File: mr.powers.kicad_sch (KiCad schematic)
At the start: 0 parts

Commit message: Place Holder:
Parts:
- added C1, C3, C4, C5: C, symbol pspice:C
- added D1: 12VAC RED, symbol Device:LED
- added D2: LED, symbol Device:LED
- added HS1: Heatsink, symbol Mechanical:Heatsink
- added R1: 100W 8Ohms, symbol Device:R
- added R2, R3, R4: 0Ω, symbol Device:R
- added R6: 1MΩ, symbol Device:R
- added R8: R, symbol Device:R
- added SW1: SW_SPST, symbol Switch:SW_SPST
- added U2: Antec 400W, symbol bvm-library:PSU
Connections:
- new net: R8.2, U2. (VDC_PSU_GND)
- new net 120VAC_SUPPLY_L: C1.1, C4.1, D1.2 (A), R2.1, R6.2
- new net 120VAC_SUPPLY_N: C1.2, C3.1, D1.1 (K), R3.1, R6.1
- new net 12VDC_SUPPLY: C5.2, U2. (VDC_PSU_GND)
- new net 3.3VDC_SUPPLY: U2. (VDC_PSU_GND)
- new net 5VDC_SB_SUPPLY: D2.2 (A), U2. (VDC_PSU_GND)
- new net 5VDC_SUPPLY: R1.1, R1.2, U2. (VDC_PSU_GND)
- new net Earth: R4.2, U2. (VDC_PSU_GND)
- new net NEUT: R3.2, U2. (VDC_PSU_GND)
- new net VAC: SW1.1 (A)
- new net VAC_GROUND: C3.2, C4.2, R4.1
- new net VAC_LINE_IN: R2.2, SW1.2 (B), U2. (VDC_PSU_GND)
- new net VDC_GND: C5.1, D2.1 (K), R8.1, U2. (VDC_PSU_GND)
- no-connect marks 2 -> 3
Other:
- sheet Mr. Power Meter renamed Mr. Power Meter Module
- added sheet 12VDC External Supply (12VDC External Supply.kicad_sch)
- note added: "-5VDC (White x1)"
- note added: "AC Power Meter of Mr Power's power. Current measurement taken before PSU using closed toroidal coil."
- note added: "DC power meter, shunted. Passes external DC power through and measurse it before passing it back out."
- note added: "FUSED"
- note added: "GFCI Will be added prior to PSU connection."
- note added: "Initial Condition Plugged in. PSU switch: Off: Everything is off, all switches in their off state. Action -> PSU Switch: On [PSU Power Switch] Result -> Ready LED turns on (GREEN) -> Always on USB charge ports 5V/2A and indicator turn on (GREEN) Action -> SYS Power: On [Top left panel] Result -> Sys Power Switch Lights Up -> System Power Monitor turns on -> Fans start -> AC Active Indicator (YELL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"
- note added: "Mr. Power Standby LED (Green)"
- note added: "PSU Mains Switch"
- note added: "PSU Needs a minimal load to before it will turn on. Is this true?"
- note added: "Since we need to modify he PSU to expose the AC lines and put a current sensor around the input AC lines, we're showing tha physical seperation between the PSU's switch and internal circuitry."
- note added: "Y Cap?"
- note added: "[AC LIVE INDICATOR]"
- note added: "https://www.smpspowersupply.com/connectors-pinouts.html"
- note added: "nPS_ON (Green x1)"
- note removed: "-5VDC ?? (White x1)"
- note removed: "120VAC_INT_SUPPLY_LIVE"
- note removed: "120VAC_INT_SUPPLY_NUETRAL"
- note removed: "AC Digital Meter (D85-2058) Hall Effect: AC 40V-300V, 0A - 100A"
- note removed: "AC Power Meter (KWS-AC300-100A) Hall Effect: AC 50V-300V 0A-100A"
- note removed: "DC Meter: (PZEM-051) Shunt: DC 6.5V-100V 0A-100A"
- note removed: "Initial Condition Pluged in. PSU switch: Off: Everything is off, all switches in their off state. Action -> PSU Switch: On Result -> Ready LED turns on -> Always on USB charge ports 5V/2A and indicator turn on Action -> SYS Power: On Result -> Switch Lights Up -> System Power Monitor turns on -> Fans start Action -> 12V Switch: On Result -> 12V monitor turns on -> 12V terminals "live" The same pa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"
- note removed: "PS_ON (Green x1)"
- note removed: "VAC_GROUND"
- note removed: "[4] DC Meter: (YB27VA) Shunt: DC 0V-100V 0A-50A"

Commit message: Draft 5VDC Supply Schematic
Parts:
- removed C5: C, symbol pspice:C
- D2: value LED -> 5VDC GREEN
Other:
- note added: "[STANDBY ACTIVE INDICATOR]"
- note removed: "Mr. Power Standby LED (Green)"

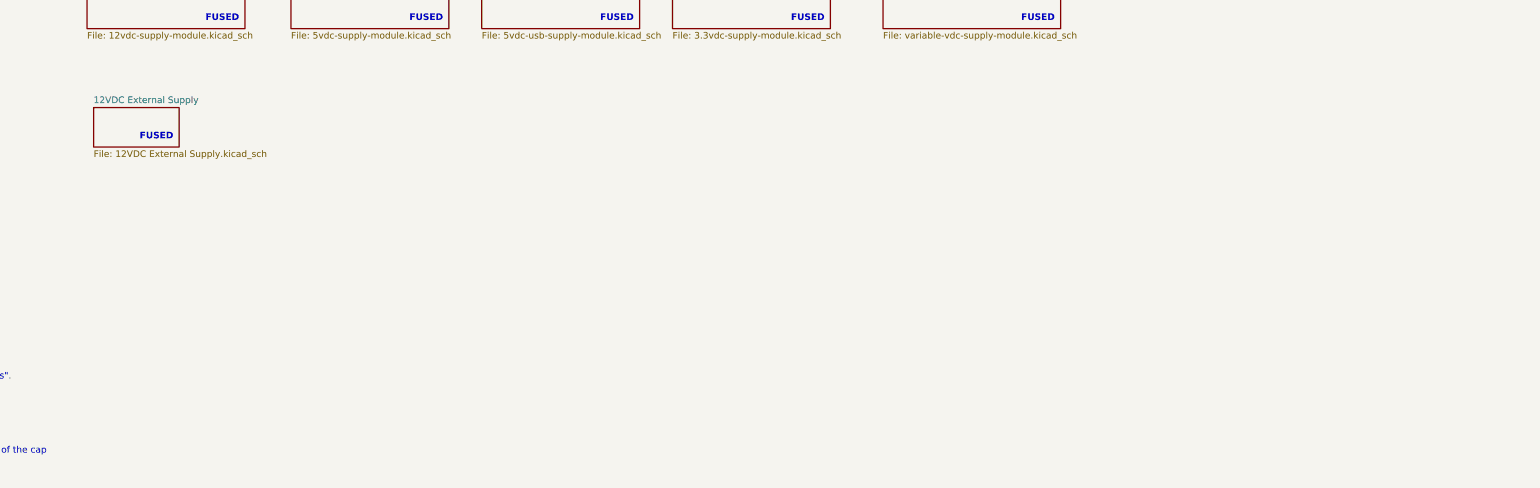
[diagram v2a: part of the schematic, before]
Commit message: Save more changes
Started Fan Control
Created VDC Meter Template
Fleshed out 12, 5, 5-usb, and 3.3 modules
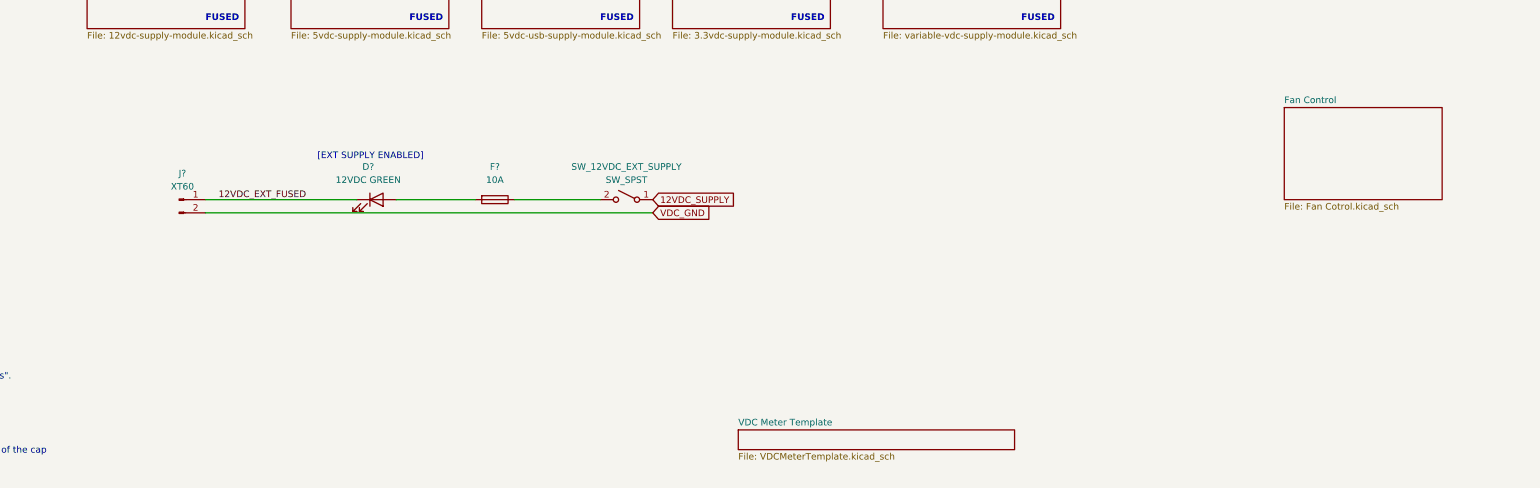
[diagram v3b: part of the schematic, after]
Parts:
- added D?: 12VDC GREEN, symbol Device:LED
- added F?: 10A, symbol Device:Fuse
- added J?: XT60, symbol Connector:Conn_01x02_Male
- added SW_12VDC_EXT_SUPPLY: SW_SPST, symbol Switch:SW_SPST
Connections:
- net 12VDC_SUPPLY: now also SW_12VDC_EXT_SUPPLY.1 (A)
- net VDC_GND: now also J?.2 (Pin_2)
- new net: F?.1, SW_12VDC_EXT_SUPPLY.2 (B)
- new net: D?.2 (A), F?.2
- new net 12VDC_EXT_FUSED: D?.1 (K), J?.1 (Pin_1)
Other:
- removed sheet 12VDC External Supply
- added sheet Fan Control (Fan Cotrol.kicad_sch)
- added sheet VDC Meter Template (VDCMeterTemplate.kicad_sch)
- note added: "[EXT SUPPLY ENABLED]"

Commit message: Bunch more changes
Blah blah
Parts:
- removed C1, C3, C4: C, symbol pspice:C
- removed D1: 12VAC RED, symbol Device:LED
- removed D2: 5VDC GREEN, symbol Device:LED
- removed D?: 12VDC GREEN, symbol Device:LED
- removed F?: 10A, symbol Device:Fuse
- removed J?: XT60, symbol Connector:Conn_01x02_Male
- removed R2, R3, R4: 0Ω, symbol Device:R
- removed R6: 1MΩ, symbol Device:R
- removed SW_12VDC_EXT_SUPPLY: SW_SPST, symbol Switch:SW_SPST
- added R? (x3): 0Ω, symbol Device:R
- R8: value R -> 0Ω
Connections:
- net 120VAC_SUPPLY_L: now also R?.2
- net 120VAC_SUPPLY_N: now also R?.2
- net Earth: now also R?.1
- net NEUT: now also R?.1
- net VAC_GROUND: now also R?.2
- net VAC_LINE_IN: now also R?.1
- net nPS_ON: now reaches R8.2, U2. (VDC_PSU_GND)
- new net -12VDC: U2. (VDC_PSU_GND)
- new net -5VDC: U2. (VDC_PSU_GND)
- new net PS_POWER_OK: U2. (VDC_PSU_GND)
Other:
- removed sheet Fan Control
- added sheet 12VDC External Supply Module (12vdc-ext-supply-module.kicad_sch)
- added sheet 5VDC USB Always On (always-on-usb.kicad_sch)
- added sheet Fan Control Module (fan-control-module.kicad_sch)
- note added: "AC Current Measured Here"
- note added: "Enhancements: - Add calibration terminals External Add-ons: - A high current or high voltage (1000V+) generator with high capacitence for _stupid_ "experiments". - 12VDC in as control for switches and relays. - 125VAC in for power. - Power Meter - Voltage/Current transformer - Voltage/current setting ability? Part of meter? - Safety toggle switch for AC power enable - a SPDT ON-OFF-ON Momentary t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"
- note removed: "Initial Condition Plugged in. PSU switch: Off: Everything is off, all switches in their off state. Action -> PSU Switch: On [PSU Power Switch] Result -> Ready LED turns on (GREEN) -> Always on USB charge ports 5V/2A and indicator turn on (GREEN) Action -> SYS Power: On [Top left panel] Result -> Sys Power Switch Lights Up -> System Power Monitor turns on -> Fans start -> AC Active Indicator (YELL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"
- note removed: "Y Cap?"
- note removed: "[EXT SUPPLY ENABLED]"
- note removed: "[STANDBY ACTIVE INDICATOR]"

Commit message: Minor change across the board
I need better notes.
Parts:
- gave numbers to parts that had none: 3
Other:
- note removed: "[AC LIVE INDICATOR]"
